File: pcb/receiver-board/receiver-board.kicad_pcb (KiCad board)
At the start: 2 copper layers, 0 parts

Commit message: Add receiver-board schematic and pcb
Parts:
- added J1: Conn_01x03_Socket, Connector_PinSocket_1.00mm:PinSocket_1x03_P1.00mm_Vertical, F.Cu at (42.5, 37.5)
- added REF**: MountingHole_2.5mm, MountingHole:MountingHole_2.5mm, F.Cu at (37.0, 39.0)
- added REF**: MountingHole_2.5mm, MountingHole:MountingHole_2.5mm, F.Cu at (50.0, 39.0)
- added REF**: MountingHole_2.5mm, MountingHole:MountingHole_2.5mm, F.Cu at (37.0, 31.0)
- added REF**: MountingHole_2.5mm, MountingHole:MountingHole_2.5mm, F.Cu at (50.0, 31.0)
- added U2: TSSP58038, OptoDevice:Vishay_MINICAST-3Pin, F.Cu at (46.0, 32.5)
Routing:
- net /GATE_TRIGGER2: track 0.00 -> 9.61 mm
- net +3V3: track 0.00 -> 5.61 mm
- net GND: track 0.00 -> 5.39 mm
- added copper zone on B.Cu, net GND

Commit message: receiver-board
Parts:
- removed the REF** at (37.0, 39.0)
- removed the REF** at (50.0, 39.0)
- J1: footprint Connector_PinSocket_1.00mm:PinSocket_1x03_P1.00mm_Vertical -> Connector_Audio:Jack_3.5mm_CUI_SJ-3523-SMT_Horizontal
- moved REF** 19.2 mm to (47.0, 50.0)
- moved J1 7.91 mm to (38.0, 44.0), turned to 180 degrees
- moved REF** 1.80 mm to (35.5, 32.0)
- moved U2 0.50 mm to (46.0, 33.0)
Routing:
- net +3V3: track 5.61 -> 15.8 mm
- net /GATE_TRIGGER2: track 9.61 -> 16.8 mm
- net GND: track 5.39 -> 6.39 mm
- added copper zone on F.Cu, net GND
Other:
- board outline added: 17.5 x 24 mm

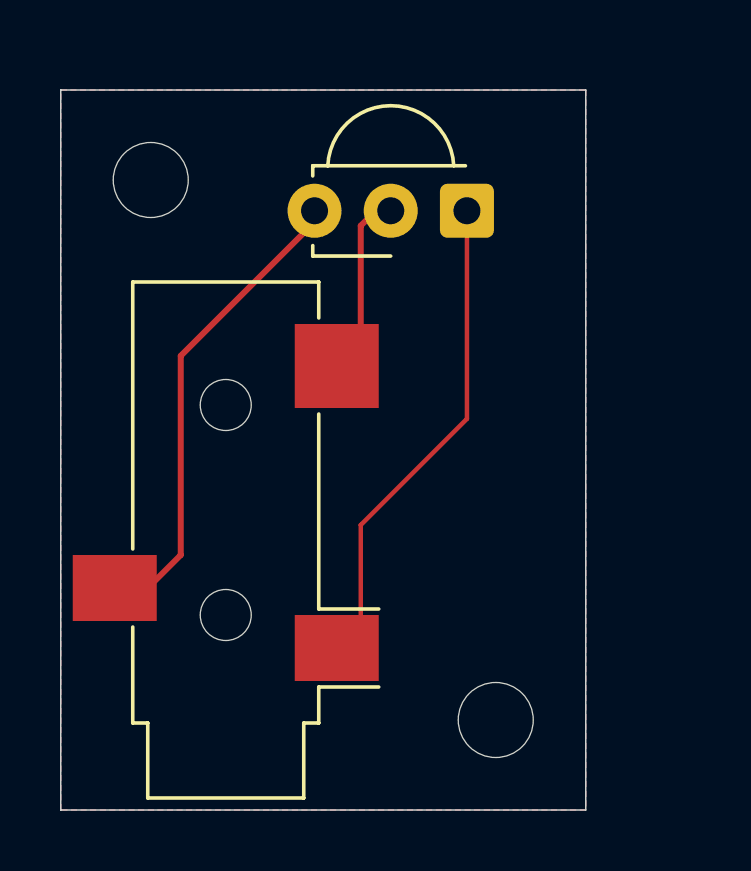
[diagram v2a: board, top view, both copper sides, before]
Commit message: Added capacitor and changed jack on receiver board
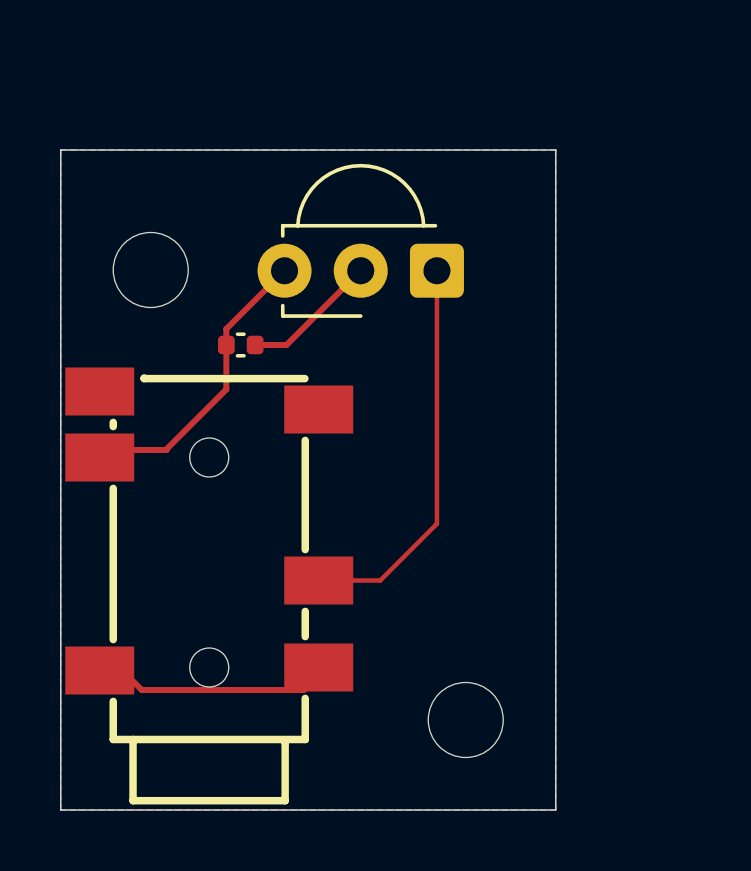
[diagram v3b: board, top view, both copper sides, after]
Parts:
- removed J1: Conn_01x03_Socket, Connector_Audio:Jack_3.5mm_CUI_SJ-3523-SMT_Horizontal
- added C6: C-1u-0402, Capacitor_SMD:C_0402_1005Metric, F.Cu at (38.5, 37.5)
- added J2: Jack_PJ-342, Connector_JAE:Jack_PJ-342, F.Cu at (37.5, 45.0)
- moved REF** 3.00 mm to (35.5, 35.0)
- moved U2 2.24 mm to (45.0, 35.0)
- moved REF** 1.00 mm to (46.0, 50.0)
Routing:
- net +3V3: track 15.8 -> 9.36 mm
- net GND: track 6.39 -> 12.6 mm
- net /GATE_TRIGGER2: track 16.8 -> 13.2 mm
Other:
- board size 17.5 x 24 mm -> 16.5 x 22 mm

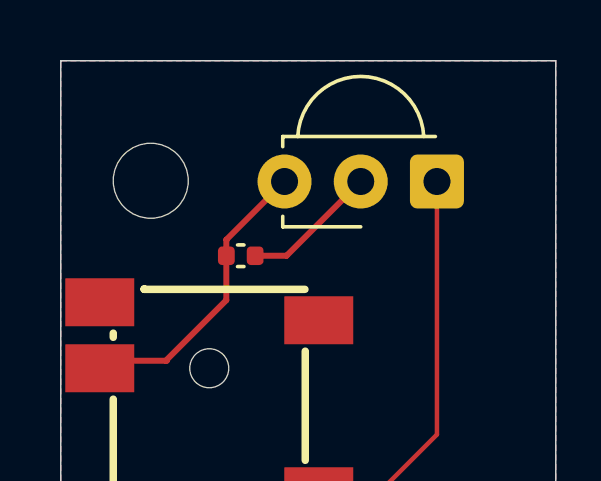
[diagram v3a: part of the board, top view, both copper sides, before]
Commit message: replace whole on receiver board
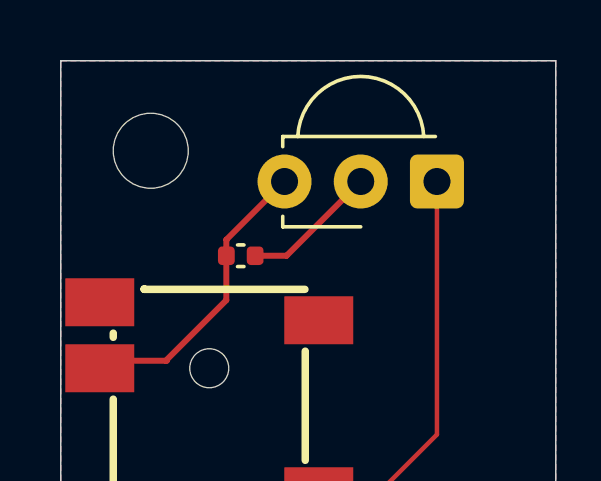
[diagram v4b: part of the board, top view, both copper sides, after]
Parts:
- moved REF** 1.00 mm to (35.5, 34.0)
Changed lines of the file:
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@@
 	(footprint "MountingHole:MountingHole_2.5mm"
 		(layer "F.Cu")
-		(at 35.5 35)
+		(at 35.5 34)
 		(descr "Mounting Hole 2.5mm, no annular, generated by kicad-footprint-generator mountinghole.py")
 		(tags "mountinghole")

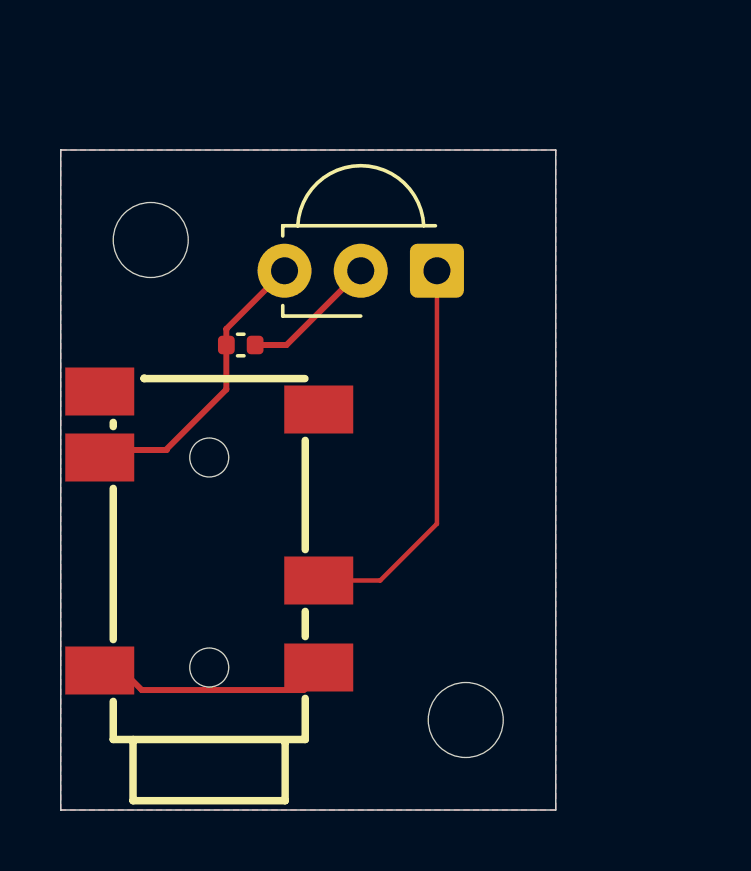
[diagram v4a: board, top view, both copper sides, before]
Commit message: Clear DRC, move audio jack and resize the board, update title block author and date
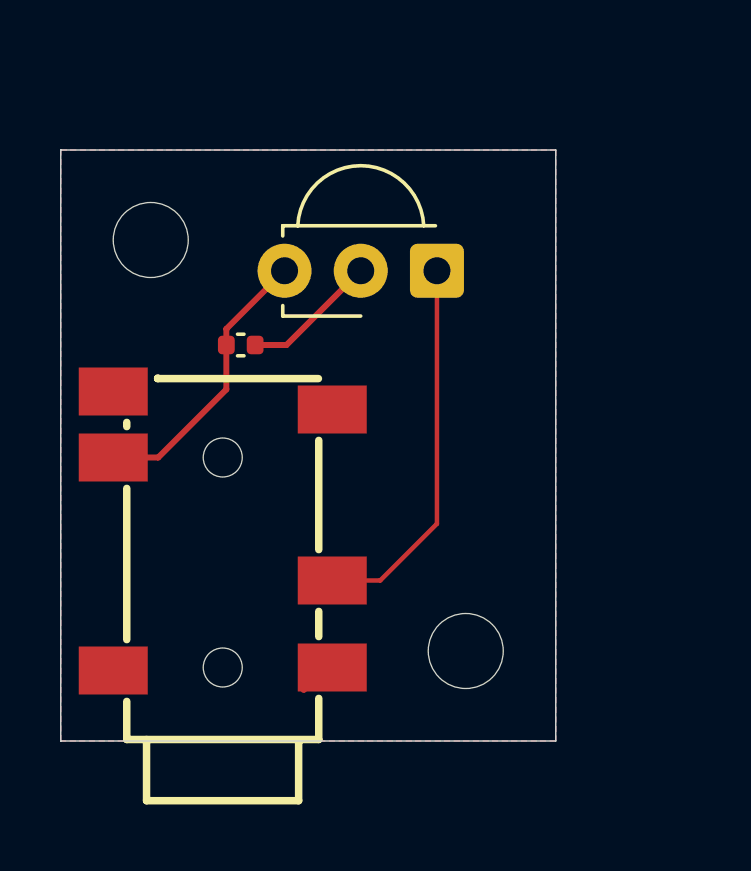
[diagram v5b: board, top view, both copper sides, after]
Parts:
- moved REF** 2.30 mm to (46.0, 47.7)
- moved J2 0.45 mm to (38.0, 45.0)
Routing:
- net GND: track 12.6 -> 5.96 mm
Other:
- board size 16.5 x 22 mm -> 16.5 x 19.7 mm
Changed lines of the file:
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@@
 	(title_block
 		(title "Lap Timer: Receiver Board")
-		(date "2025-10-19")
+		(date "2025-11-09")
 		(rev "1.0.0")
-		(comment 1 "Project author: <author>")
+		(comment 1 "Project author: Radosław Mierzwa")
 	)
 	(layers
@@
 	(footprint "MountingHole:MountingHole_2.5mm"
 		(layer "F.Cu")
-		(at 46 50)
+		(at 46 47.7)
 		(descr "Mounting Hole 2.5mm, no annular, generated by kicad-footprint-generator mountinghole.py")
 		(tags "mountinghole")
@@
 	(footprint "Connector_JAE:Jack_PJ-342"
 		(layer "F.Cu")
-		(at 37.5 45 180)
+		(at 37.95 45 180)
 		(property "Reference" "J2"
 			(at 0 -0.5 180)
@@
 	(gr_rect
 		(start 32.5 31)
-		(end 49 53)
+		(end 49 50.7)
 		(stroke
 			(width 0.05)
@@
 		(fill no)
 		(layer "Edge.Cuts")
-	)
-	(segment
-		(start 35.201 49.001)
-		(end 34.3 48.1)
-		(width 0.2)
-		(layer "F.Cu")
-		(net 1)
-	)
-	(segment
-		(start 40.599 49.001)
-		(end 35.201 49.001)
-		(width 0.2)
-		(layer "F.Cu")
-		(net 1)
 	)
 	(segment
@@
 	(segment
 		(start 43.15 45.35)
+		(end 41.55 45.35)
+		(width 0.15)
+		(layer "F.Cu")
+		(net 2)
+	)
+	(segment
+		(start 43.15 45.35)
 		(end 45.04 43.46)
 		(width 0.15)
@@
 	)
 	(segment
-		(start 41.1 45.35)
-		(end 43.15 45.35)
-		(width 0.15)
-		(layer "F.Cu")
-		(net 2)
-	)
-	(segment
 		(start 38.02 37.5)
 		(end 38.02 36.965)
-		(width 0.2)
-		(layer "F.Cu")
-		(net 3)
-	)
-	(segment
-		(start 34.3 41)
-		(end 36 41)
 		(width 0.2)
 		(layer "F.Cu")
@@
 	)
 	(segment
-		(start 36 41)
-		(end 36.04 41)
+		(start 35.75 41.25)
+		(end 34.25 41.25)
 		(width 0.2)
 		(layer "F.Cu")
@@
 	(segment
 		(start 38.02 38.98)
-		(end 36 41)
+		(end 35.75 41.25)
 		(width 0.2)
 		(layer "F.Cu")
@@
 		(polygon
 			(pts
-				(xy 32.5 31) (xy 49 31) (xy 49 53) (xy 32.5 53)
-			)
-		)
+				(xy 32.5 31) (xy 49 31) (xy 49 50.7) (xy 32.5 50.7)
+			)
+		)
